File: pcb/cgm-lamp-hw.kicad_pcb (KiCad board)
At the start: 2 copper layers, 55 parts, among them J1 USB_C_Receptacle_USB2.0_14P, J2 Conn_01x02, J3 DNP, Q1 DMG2305, SW1 RotaryEncoder_Switch_MP, SW2 SW_Push, SW3 SW_Push, SW4 SW_SPST, U1 RT9080-33GJ5, U2 MCP73831-2-OT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

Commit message: some layout
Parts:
- moved D3 182.6 mm to (61.0, 110.0), turned to 90 degrees
- moved D2 177.3 mm to (65.9, 96.2), turned to 45 degrees
- moved D4 177.0 mm to (67.5, 124.6), turned to 135 degrees
- moved D6 165.3 mm to (91.1, 123.6), turned to -135 degrees
- moved D5 164.6 mm to (80.0, 131.1), turned to 180 degrees
- moved D1 163.3 mm to (80.0, 91.0)
- moved D8 157.7 mm to (93.4, 96.2), turned to -45 degrees
- moved D7 153.6 mm to (99.0, 110.0), turned to -90 degrees
- moved D13 120.4 mm to (103.1, 138.6), turned to 135 degrees
- moved SW4 119.1 mm to (84.0, 143.2), turned to 180 degrees
- moved D12 117.5 mm to (104.9, 136.8), turned to 135 degrees
- moved R17 116.9 mm to (100.0, 135.6), turned to 135 degrees
- moved C2 115.2 mm to (83.2, 138.2), turned to 180 degrees
- moved D11 114.6 mm to (106.8, 134.9), turned to 135 degrees
- moved R16 113.7 mm to (101.8, 133.7), turned to 135 degrees
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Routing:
- net +3V3: track 0.00 -> 17.5 mm
- net /ESP_EN: track 0.00 -> 12.4 mm
- net Net-(D6-DOUT): track 0.00 -> 12.4 mm
- net Net-(D3-DOUT): track 0.00 -> 12.4 mm
- net Net-(D10-K): track 0.00 -> 11.8 mm
- net Net-(D1-DOUT): track 0.00 -> 11.4 mm
- net Net-(D7-DOUT): track 0.00 -> 11.2 mm
- net Net-(D2-DOUT): track 0.00 -> 10.9 mm
- net /BOOT: track 0.00 -> 10.9 mm
- net Net-(D4-DOUT): track 0.00 -> 10.5 mm
- net Net-(D5-DOUT): track 0.00 -> 9.31 mm
- net VBUS: track 0.00 -> 8.70 mm
- net /VREG_EN: track 0.00 -> 7.37 mm
- net /SCL: track 0.00 -> 7.18 mm
- net GND: track 0.00 -> 6.22 mm
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- added copper zone on In1.Cu, net +3V3
- added copper zone on B.Cu, net GND
- added copper zone on F.Cu, net GND
- added copper zone on In2.Cu, net GND
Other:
- board outline added: 80 x 80 mm
- copper layers 2 -> 4

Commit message: mdns
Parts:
- moved J2 16.8 mm to (112.0, 97.6), turned to 110 degrees
- moved Q1 3.88 mm to (103.7, 93.3), turned to -90 degrees
- moved D10 3.08 mm to (100.9, 93.3)
- moved C4 2.20 mm to (100.7, 97.2), turned to -90 degrees
- moved R5 1.74 mm to (101.6, 90.3)
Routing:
- net /IND: track 0.00 -> 60.3 mm, vias 0 -> 2
- net /ALERT: track 1.88 -> 51.0 mm, vias 0 -> 2
- net VBUS: track 8.70 -> 39.7 mm, vias 0 -> 4
- net /VBAT: track 4.51 -> 33.4 mm, vias 0 -> 2
- net +3V3: track 17.5 -> 41.9 mm, vias 0 -> 16
- net /CHG: track 0.00 -> 18.5 mm, vias 0 -> 2
- net /RGB: track 2.94 -> 19.7 mm, vias 0 -> 1
- net /SDA: track 3.85 -> 7.01 mm
- net Net-(D10-K): track 11.8 -> 10.4 mm
- net GND: vias 0 -> 6
- net (no net): vias 1 -> 0

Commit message: More layout
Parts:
- moved D9 52.3 mm to (103.4, 81.0), turned to 45 degrees
- moved D13 52.2 mm to (109.0, 86.7), turned to -135 degrees
- moved D12 51.9 mm to (107.1, 84.9), turned to -135 degrees
- moved D11 51.9 mm to (105.2, 83.0), turned to -135 degrees
- moved R17 46.2 mm to (106.0, 89.7), turned to -135 degrees
- moved R3 46.2 mm to (100.4, 84.1), turned to -135 degrees
- moved R16 45.8 mm to (104.0, 87.9), turned to -135 degrees
- moved R15 45.6 mm to (102.1, 86.1), turned to -135 degrees
- moved J2 37.6 mm to (104.3, 134.4), turned to 45 degrees
- moved U4 18.9 mm to (108.2, 101.2), turned to 0 degrees
- moved C5 16.1 mm to (105.5, 101.2), turned to -90 degrees
- moved R7 15.1 mm to (108.2, 98.6), turned to 0 degrees
- moved R6 11.6 mm to (95.4, 109.9)
- moved C1 11.6 mm to (105.5, 97.7)
- moved C4 11.6 mm to (98.1, 108.5)
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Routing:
- net /IND: track 60.3 -> 1.86 mm, vias 2 -> 1
- net /ALERT: track 51.0 -> 14.3 mm
- net /VBAT: track 33.4 -> 48.4 mm, vias 2 -> 0
- net GND: track 6.22 -> 17.8 mm, vias 6 -> 10
- net +3V3: track 41.9 -> 31.5 mm, vias 16 -> 19
- net /CHG: track 18.5 -> 14.4 mm, vias 2 -> 0
- net /SDA: track 7.01 -> 4.05 mm
- net /SCL: track 7.18 -> 4.77 mm

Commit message: layout
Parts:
- moved TP2 2.20 mm to (65.0, 86.2)
- moved TP1 2.10 mm to (65.0, 81.7)
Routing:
- net /ESP_EN: track 12.4 -> 60.2 mm, vias 0 -> 2
- net /ENC_B: track 4.85 -> 42.8 mm, vias 0 -> 2
- net /ENC_A: track 4.90 -> 37.7 mm, vias 0 -> 2
- net /VREG_EN: track 7.37 -> 40.0 mm
- net /SDA: track 4.05 -> 34.6 mm
- net /SCL: track 4.77 -> 32.4 mm
- net /ENC_BTN: track 4.50 -> 24.0 mm, vias 0 -> 2
- net /IND: track 1.86 -> 20.3 mm, vias 1 -> 2
- net /BOOT: track 10.9 -> 29.0 mm
- net VBUS: track 39.7 -> 52.9 mm, vias 4 -> 5
- net /CHG: track 14.4 -> 26.7 mm, vias 0 -> 2
- net Net-(U3-RXD0/GPIO17): track 4.83 -> 7.05 mm
- net Net-(U3-TXD0/GPIO16): track 4.71 -> 6.79 mm

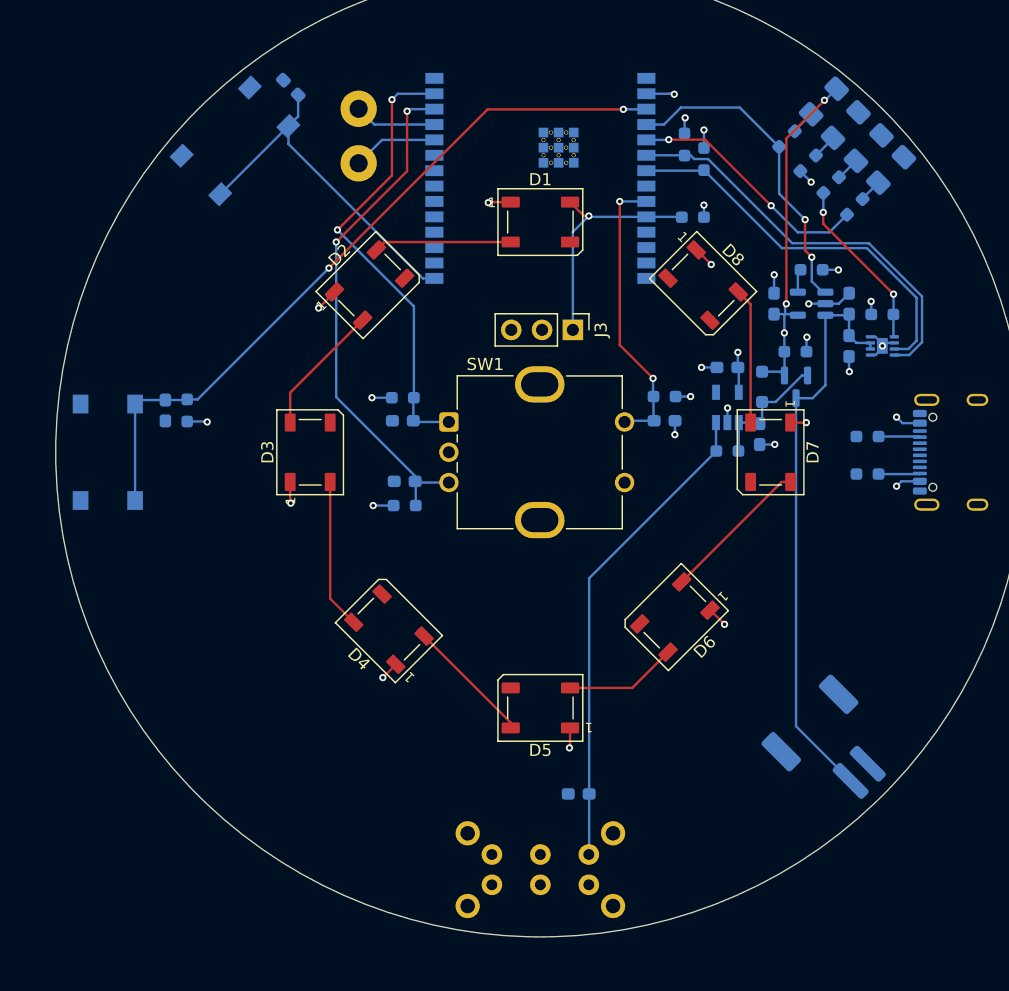
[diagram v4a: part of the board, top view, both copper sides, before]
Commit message: Add dru, more layout
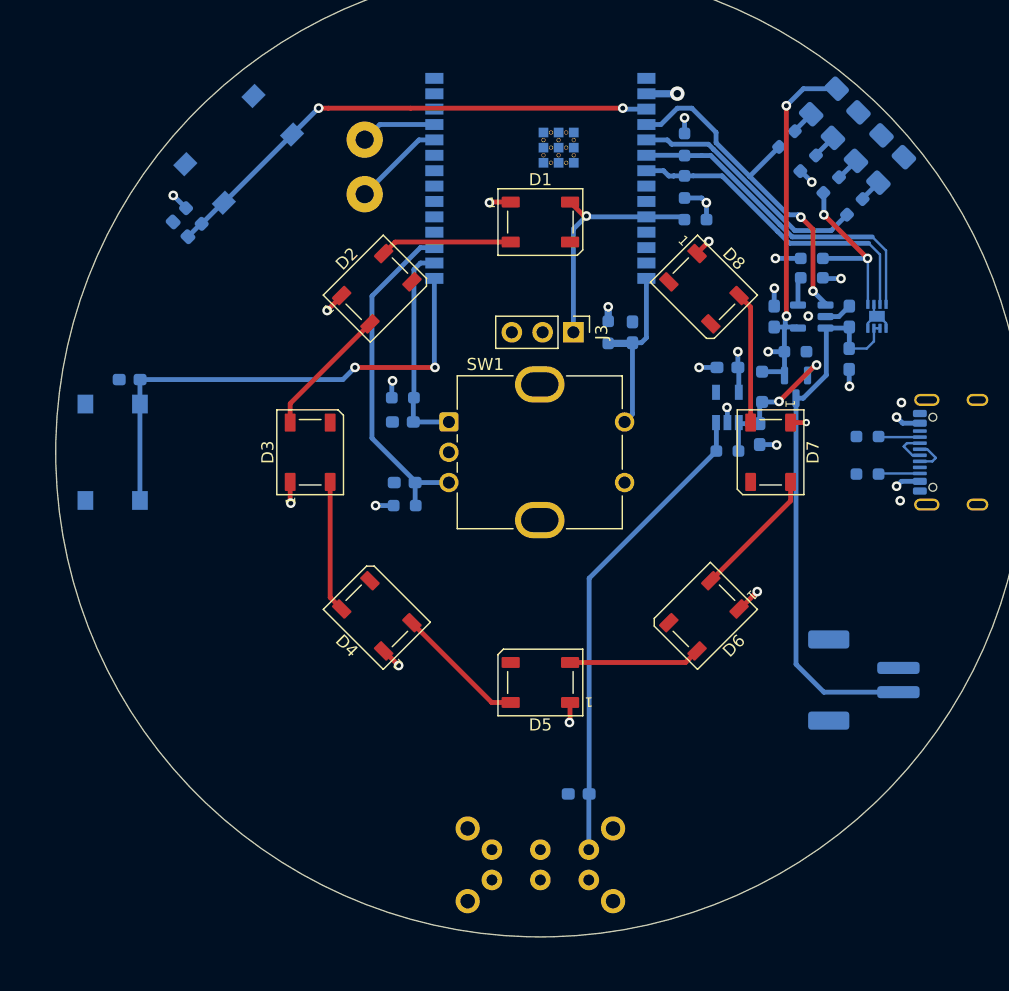
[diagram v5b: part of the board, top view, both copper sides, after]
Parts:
- moved SW3 27.6 mm to (44.7, 110.0), turned to -90 degrees
- moved C7 27.5 mm to (46.1, 104.0), turned to 180 degrees
- moved SW2 27.2 mm to (55.1, 85.0), turned to -135 degrees
- moved R10 16.1 mm to (51.4, 90.5), turned to 135 degrees
- moved C6 15.0 mm to (50.3, 91.6), turned to 135 degrees
- moved C8 7.77 mm to (87.6, 100.1), turned to -90 degrees
- moved R7 7.44 mm to (102.4, 94.0)
- moved R11 7.05 mm to (85.6, 100.1), turned to 90 degrees
- moved J2 6.09 mm to (106.7, 128.8), turned to 90 degrees
- moved R9 2.80 mm to (91.9, 88.1), turned to -90 degrees
- moved TP1 2.60 mm to (65.5, 84.2)
- moved TP2 2.60 mm to (65.5, 88.7)
- moved U4 2.48 mm to (107.8, 98.8), turned to 90 degrees
- moved D6 2.40 mm to (93.5, 123.5)
- moved D5 2.10 mm to (80.0, 129.0)
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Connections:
- U3 pad 14: unconnected-(U3-IO13-Pad14) -> /ENC_BTN
- U3 pad 16: unconnected-(U3-IO18-Pad16) -> /ENC_A
- U3 pad 17: unconnected-(U3-IO19-Pad17) -> /ENC_B
- U3 pad 26: /ENC_B -> unconnected-(U3-IO3-Pad26)
- U3 pad 27: /ENC_A -> unconnected-(U3-IO2-Pad27)
- U3 pad 9: /ENC_BTN -> unconnected-(U3-IO1-Pad9)
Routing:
- net /ENC_A: track 37.7 -> 17.5 mm, vias 2 -> 0
- net /ESP_EN: track 60.2 -> 42.3 mm
- net /ENC_B: track 42.8 -> 28.4 mm, vias 2 -> 0
- net /BOOT: track 29.0 -> 42.1 mm, vias 0 -> 2
- net /ENC_BTN: track 24.0 -> 15.0 mm, vias 2 -> 0
- net /SDA: track 34.6 -> 27.5 mm
- net /SCL: track 32.4 -> 26.3 mm
- net /D-: track 0.00 -> 3.08 mm
- net /D+: track 0.00 -> 3.02 mm
- net GND: track 17.8 -> 14.8 mm, vias 10 -> 9
- net Net-(D10-K): track 10.4 -> 13.1 mm, vias 0 -> 2
- net /CHG: track 26.7 -> 29.1 mm
- net /VBAT: track 48.4 -> 46.2 mm
- net VBUS: track 52.9 -> 54.7 mm
- net Net-(D5-DOUT): track 9.31 -> 10.9 mm
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
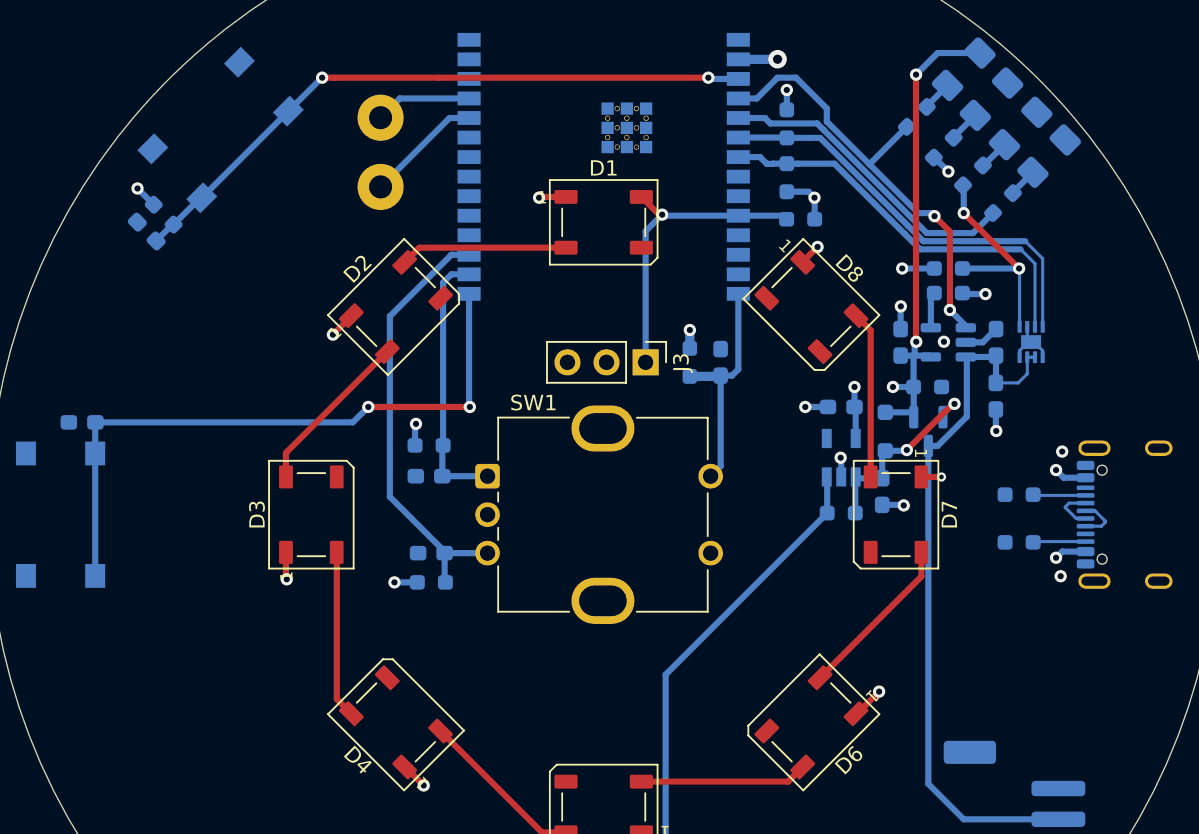
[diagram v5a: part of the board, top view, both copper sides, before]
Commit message: Tweak footprints for drc, route USB
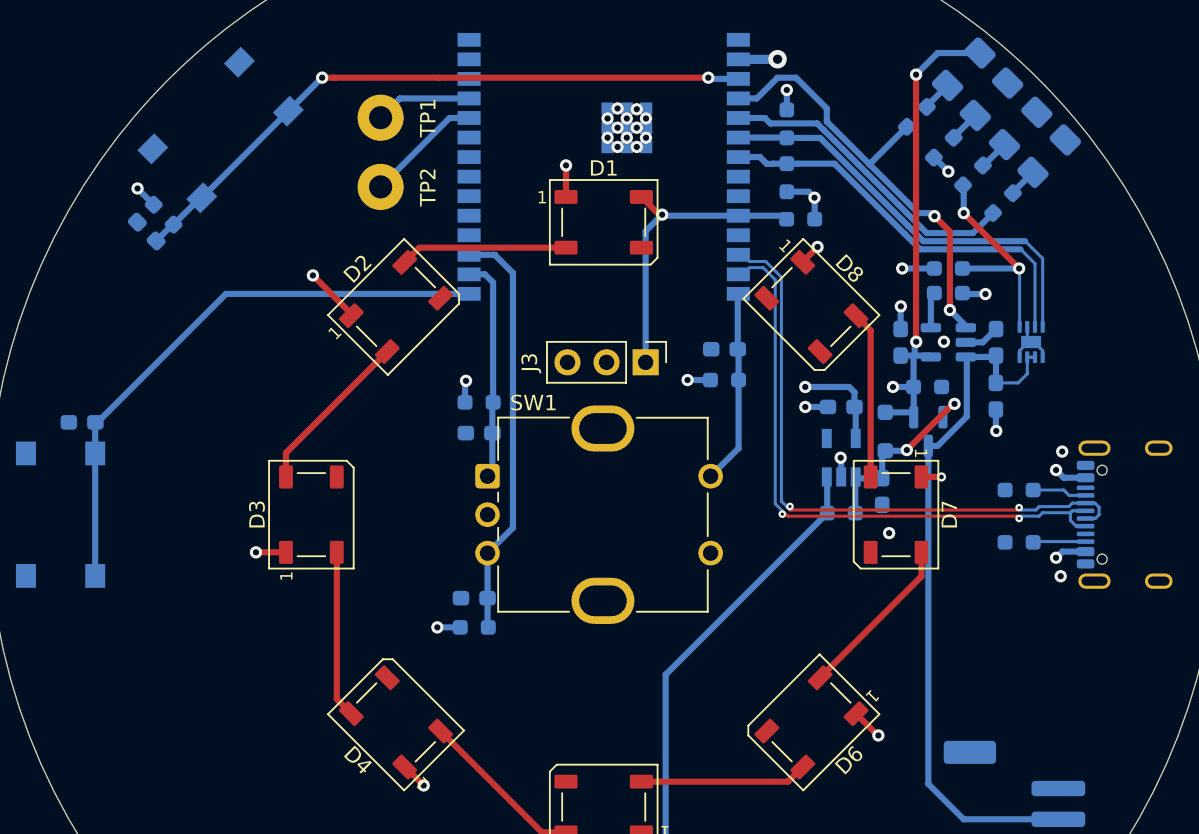
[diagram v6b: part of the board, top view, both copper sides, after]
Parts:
- moved C10 4.29 mm to (71.9, 104.7)
- moved R13 4.29 mm to (71.9, 102.7)
- moved C11 4.04 mm to (71.6, 115.4)
- moved R14 4.04 mm to (71.6, 117.3)
- moved R11 2.53 mm to (87.8, 101.2), turned to 180 degrees
- moved C8 0.89 mm to (87.8, 99.2), turned to 0 degrees
- moved R2 0.30 mm to (107.0, 108.4)
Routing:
- net /D-: track 3.08 -> 40.9 mm, vias 0 -> 2
- net /D+: track 3.02 -> 40.6 mm, vias 0 -> 2
- net +3V3: track 33.0 -> 38.7 mm
- net /BOOT: track 42.1 -> 37.7 mm, vias 2 -> 0
- net /ENC_A: track 17.5 -> 14.5 mm
- net /ENC_BTN: track 15.0 -> 12.6 mm
- net GND: track 14.8 -> 13.4 mm, vias 9 -> 21
- net /ENC_B: track 28.4 -> 27.1 mm
